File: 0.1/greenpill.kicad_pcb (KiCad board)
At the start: 4 copper layers, 20 x 55.1 mm, 31 parts, among them J1 Conn_01x20_Male, J2 Conn_01x20_Male, J3 Conn_01x04_Male, J5 USB_C_Receptacle_USB2.0, SW1 SW_Push, SW2 SW_Push, U1 ATSAMD51G18A-M, U2 MIC5504-3.3YM5, U3 S25FL064, Y1 Crystal_GND23

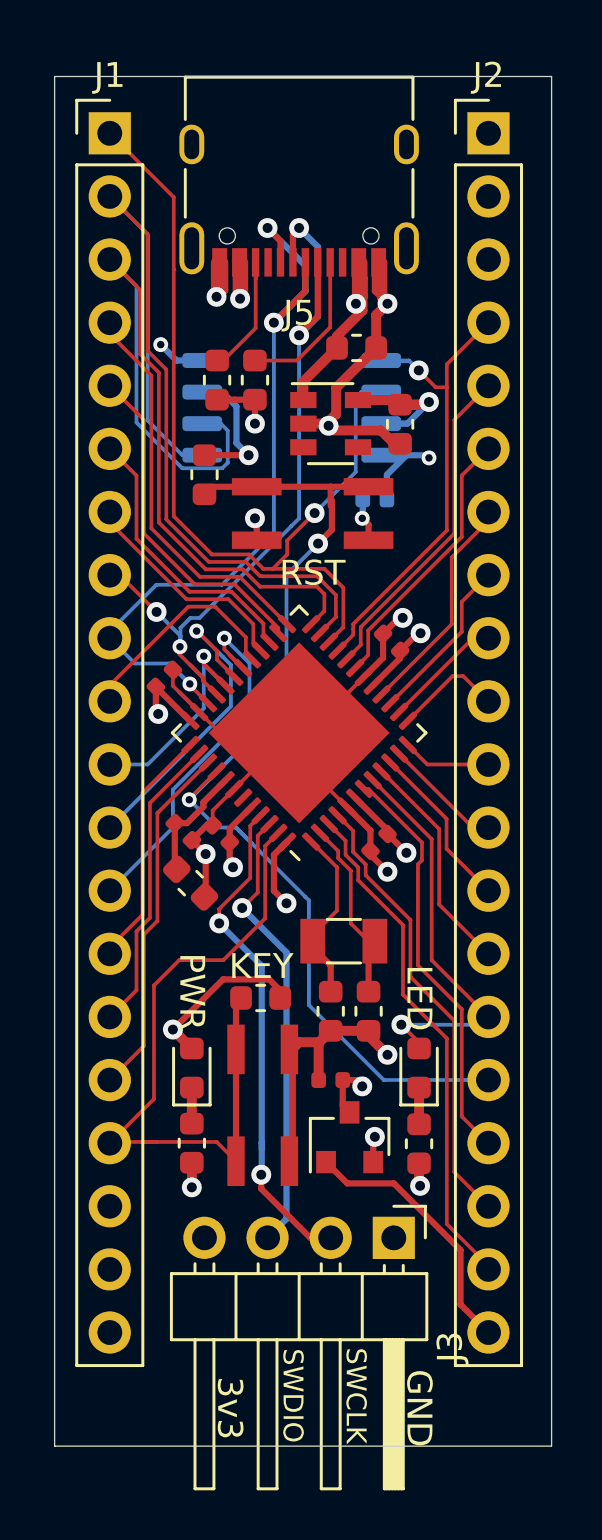
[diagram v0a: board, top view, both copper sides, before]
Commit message: Trimmed board, added pinout silkscreen
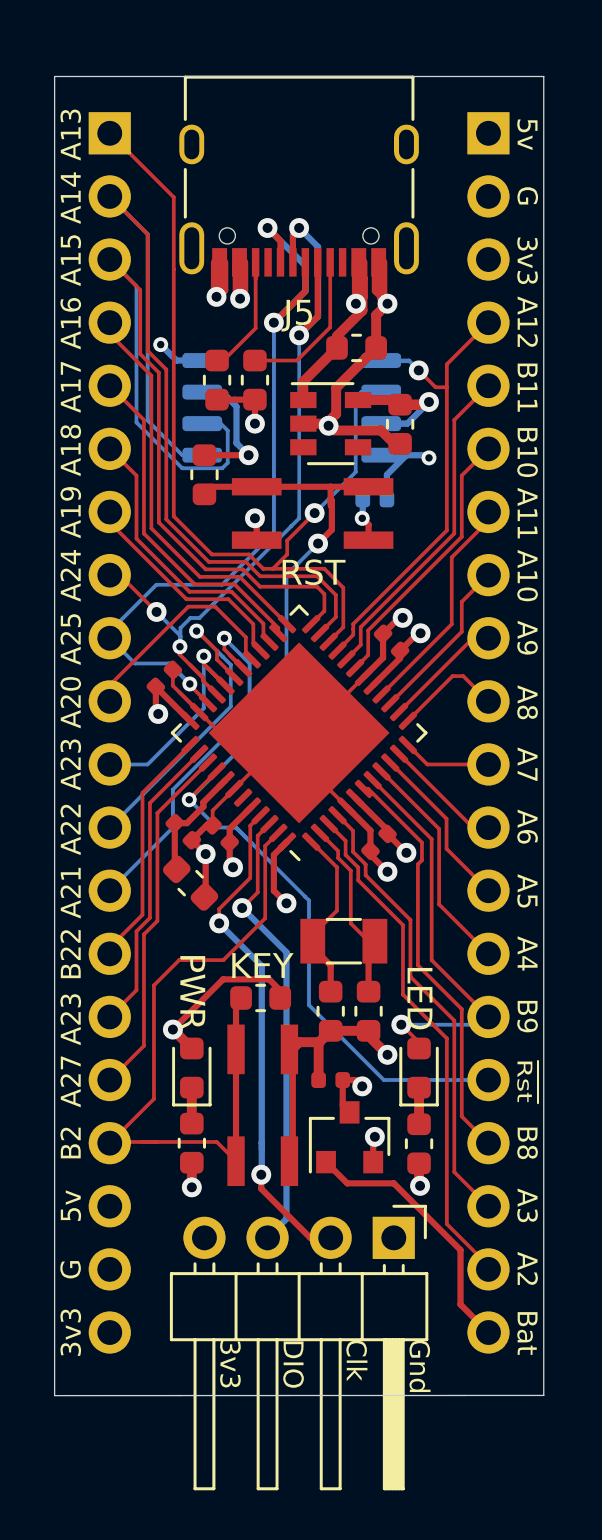
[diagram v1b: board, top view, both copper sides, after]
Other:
- board size 20 x 55.1 mm -> 19.7 x 53.1 mm
- board text added: "5v"
- board text added: "A10"
- board text added: "A11"
- board text added: "A12"
- board text added: "A13"
- board text added: "A14"
- board text added: "A15"
- board text added: "A16"
- board text added: "A17"
- board text added: "A18"
- board text added: "A19"
- board text added: "A2"
- board text added: "A20"
- board text added: "A21"
- board text added: "A22"
- board text added: "A23"
- board text added: "A24"
- board text added: "A25"
- board text added: "A27"
- board text added: "A3"
- board text added: "A4"
- board text added: "A5"
- board text added: "A6"
- board text added: "A7"
- board text added: "A8"
- board text added: "A9"
- board text added: "B10"
- board text added: "B11"
- board text added: "B2"
- board text added: "B22"
- board text added: "B8"
- board text added: "B9"
- board text added: "Bat"
- board text added: "Clk"
- board text added: "DIO"
- board text added: "G"
- board text added: "Gnd"
- board text added: "Rst"
- board text removed: "GND"
- board text removed: "SWCLK"
- board text removed: "SWDIO"

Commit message: PINOUT CHANGE, rerouted and updated silk.s
Swapped left pins 13 and 16 (formerly A21 & A27 respectively) so PWM output on A21 can be used for Textier LED4:G. A27 now on pin L13 is used for key matrix scanning and so doesn't require PWM
Rerouted only affected traces
Swapped silkscreen labels
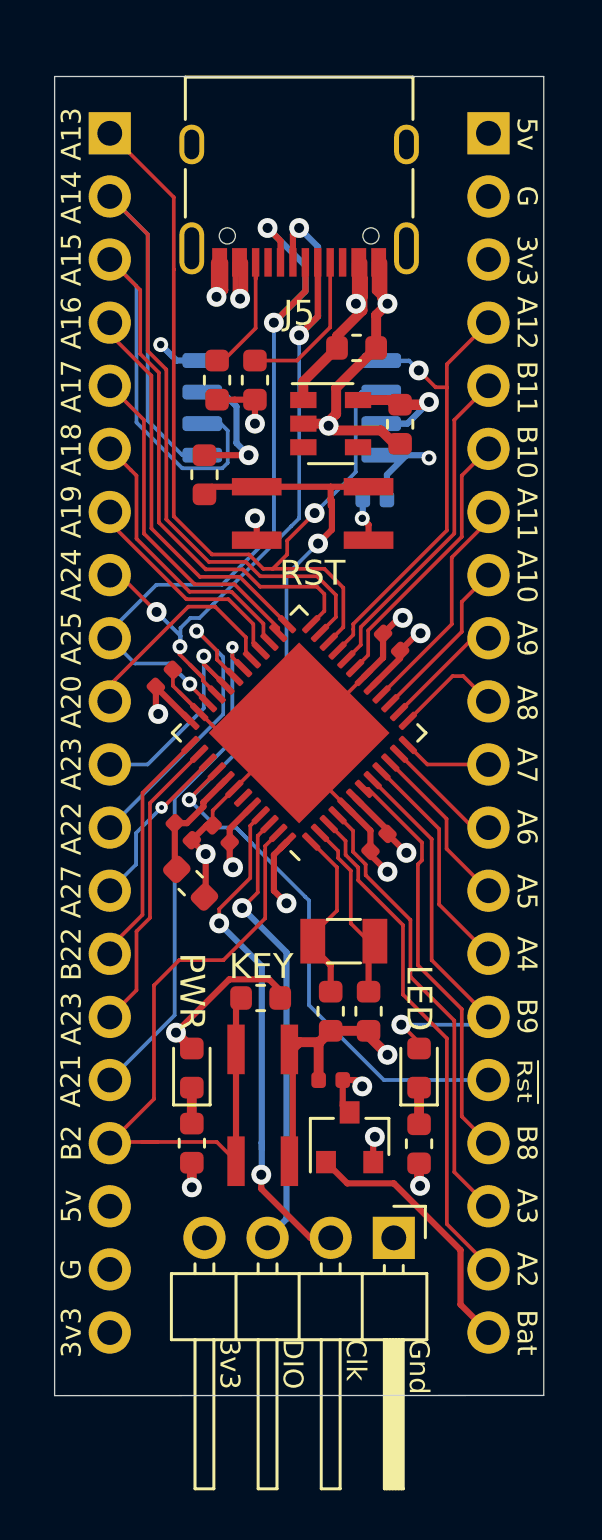
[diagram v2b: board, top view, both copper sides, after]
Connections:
- J1 pad 13: /pa21 -> /pa27
- J1 pad 16: /pa27 -> /pa21
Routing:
- net /pa27: track 14.4 -> 6.89 mm, vias 0 -> 1
- net /pa21: track 15.2 -> 20.5 mm
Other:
- net class Default: clearance 0.15 -> 0.09; trace_width 0.25 -> 0.09; via_dia 0.8 -> 0.5; via_drill 0.4 -> 0.2
- rule trace_clearance: 0.15 -> 0.09
- rule trace_min: 0.127 -> 0.09
- rule via_min_drill: 0.3 -> 0.2
- rule via_min_size: 0.4 -> 0.45

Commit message: a bit of tweaking
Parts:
- C7, C8: value 1u -> 10u
- moved R2 7.70 mm to (140.0, 83.0)
- moved U2 4.89 mm to (132.7, 83.4), turned to 270 degrees
- moved R1 4.71 mm to (138.4, 83.0)
- moved C8 3.92 mm to (136.1, 84.4), turned to 0 degrees
- moved C7 1.97 mm to (136.1, 82.2)
- moved SW1 1.46 mm to (136.4, 88.0)
- moved R5 0.23 mm to (132.0, 87.7), turned to 90 degrees
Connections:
- R6 pad 2: /pb02 -> /pa02
- SW2 pad 1: /pb02 -> /pa02
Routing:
- net /pa02: track 20.6 -> 42.1 mm, vias 0 -> 1
- net /cc2: track 5.16 -> 15.2 mm
- net /pb02: track 29.3 -> 26.3 mm
- net /pa12: track 20.0 -> 21.8 mm, vias 1 -> 0
- net +3V3: track 123.4 -> 125.2 mm, vias 9 -> 10
- net /pa25: track 33.0 -> 31.5 mm
- net /pa13: track 36.3 -> 37.7 mm
- net /pa24: track 32.3 -> 31.1 mm
- net /cc1: track 5.94 -> 5.06 mm
- net /pa15: track 34.6 -> 34.0 mm
- net +5V: track 66.4 -> 67.0 mm, vias 2 -> 3
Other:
- board text added: "1"
- board text added: "10"
- board text added: "11"
- board text added: "12"
- board text added: "13"
- board text added: "14"
- board text added: "15"
- board text added: "16"
- board text added: "17"
- board text added: "18"
- board text added: "19"
- board text added: "2"
- board text added: "20"
- board text added: "21"
- board text added: "22"
- board text added: "23"
- board text added: "24"
- board text added: "25"
- board text added: "26"
- board text added: "27"
- board text added: "28"
- board text added: "29"
- board text added: "3"
- board text added: "30"
- board text added: "31"
- board text added: "32"
- board text added: "4"
- board text added: "5"
- board text added: "6"
- board text added: "7"
- board text added: "8"
- board text added: "9"

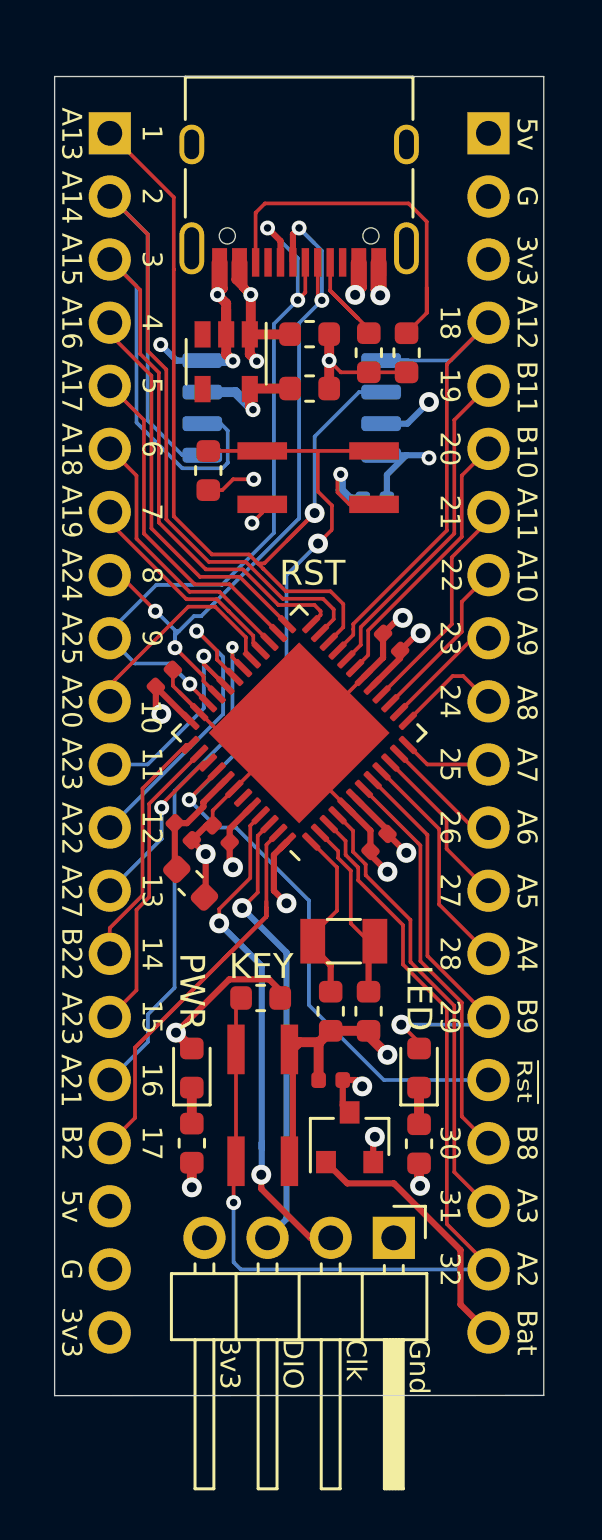
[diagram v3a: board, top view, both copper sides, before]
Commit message: Switched to QFN-64 package, reassigned pins. Trimmed Edge.Cuts
Still TODO:
 - Redo silkscreen
 - Move passives near MCU to optimal position (1v2 caps especially)
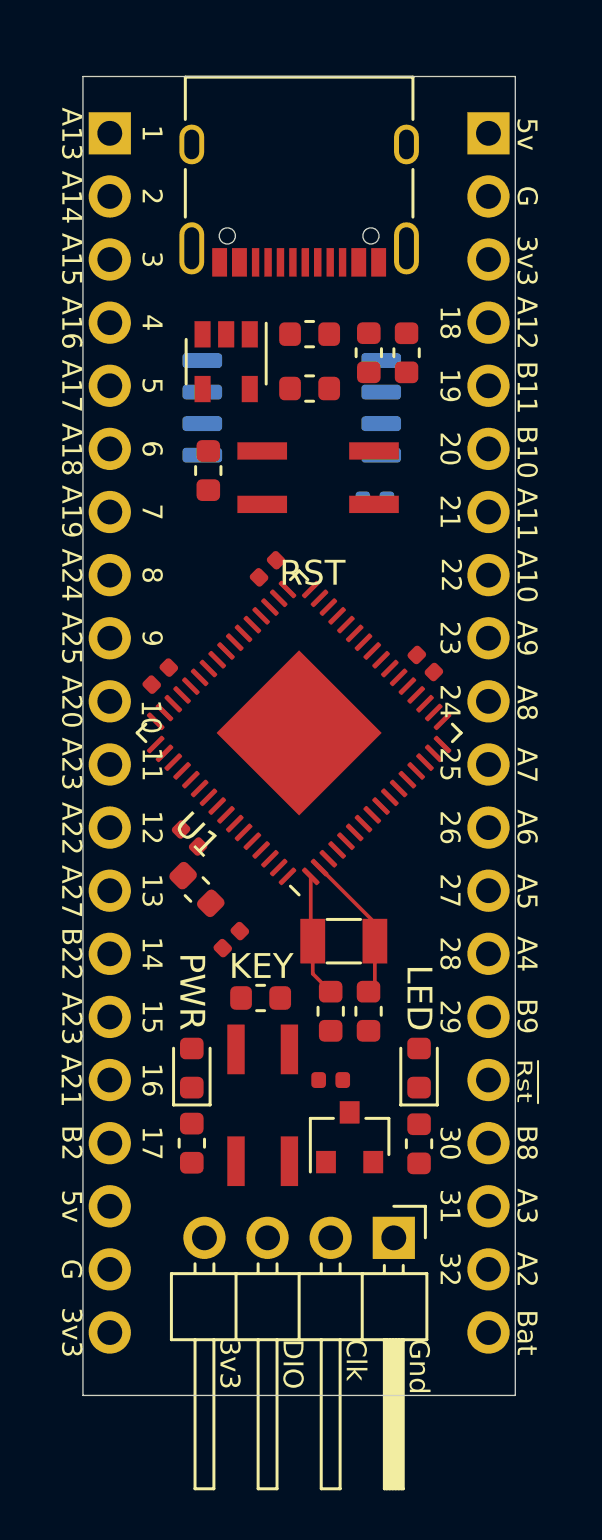
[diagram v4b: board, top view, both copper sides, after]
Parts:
- U1: value ATSAMD51G18A-M -> ATSAMD51J18A-M; footprint Package_DFN_QFN:QFN-48-1EP_7x7mm_P0.5mm_EP5.15x5.15mm -> Package_DFN_QFN:QFN-64-1EP_9x9mm_P0.5mm_EP4.7x4.7mm
- moved C4 11.1 mm to (130.0, 96.0), turned to 45 degrees
- moved C1 6.06 mm to (134.4, 91.7)
- moved C2 4.27 mm to (132.9, 106.6), turned to 225 degrees
- moved C6 1.60 mm to (140.7, 95.5)
- moved C5 0.36 mm to (131.5, 104.6)
- moved C3 0.36 mm to (131.2, 102.5)
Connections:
- D2 pad 2: /pb09 -> /pb04
- J1 pad 1: /pa13 -> /pa16
- J1 pad 10: /pa20 -> /pa22
- J1 pad 11: /pa23 -> /pb22
- J1 pad 12: /pa22 -> /pb23
- J1 pad 14: /pb22 -> /pb31
- J1 pad 15: /pb23 -> /pb00
- J1 pad 16: /pa21 -> /pb01
- J1 pad 2: /pa14 -> /pa17
- J1 pad 3: /pa15 -> /pa18
- J1 pad 4: /pa16 -> /pa19
- J1 pad 5: /pa17 -> /pb16
- J1 pad 6: /pa18 -> /pb17
- J1 pad 7: /pa19 -> /pa20
- J2 pad 15: /pb09 -> /pa02
- J2 pad 17: /pb08 -> /pb30
- J2 pad 19: /pa02 -> /pb04
- J2 pad 4: /pa12 -> /pb13
- J2 pad 5: /pb11 -> /pb12
- J2 pad 6: /pb10 -> /pb11
- J2 pad 7: /pa11 -> /pb10
- U1 pad 10: /pa05 -> /pb07
- U1 pad 11: /pa06 -> /pb08
- U1 pad 12: /pa07 -> /pb09
- U1 pad 13: /pa08 -> /pa04
- U1 pad 14: /pa09 -> /pa05
- U1 pad 15: /pa10 -> /pa06
- U1 pad 16: /pa11 -> /pa07
- U1 pad 17: +3V3 -> /pa08
- U1 pad 18: GND -> /pa09
- U1 pad 19: /pb10 -> /pa10
- U1 pad 20: /pb11 -> /pa11
- U1 pad 21: /pa12 -> +3V3
- U1 pad 22: /pa13 -> GND
- U1 pad 23: /pa14 -> /pb10
- U1 pad 24: /pa15 -> /pb11
- U1 pad 25: /pa16 -> /pb12
- U1 pad 26: /pa17 -> /pb13
- U1 pad 27: /pa18 -> /pb14
- U1 pad 28: /pa19 -> /pb15
- U1 pad 29: /pa20 -> /pa12
- U1 pad 30: /pa21 -> /pa13
- U1 pad 31: /pa22 -> /pa14
- U1 pad 32: /pa23 -> /pa15
- U1 pad 33: /pa24 -> GND
- U1 pad 34: /pa25 -> +3V3
- U1 pad 35: GND -> /pa16
- U1 pad 36: +3V3 -> /pa17
- U1 pad 37: /pb22 -> /pa18
- U1 pad 38: /pb23 -> /pa19
- U1 pad 39: /pa27 -> /pb16
- U1 pad 40: /!reset -> /pb17
- U1 pad 41: +1V2 -> /pa20
- U1 pad 42: GND -> /pa21
- U1 pad 43: /vsw -> /pa22
- U1 pad 44: +3V3 -> /pa23
- U1 pad 45: /pa30 -> /pa24
- U1 pad 46: /pa31 -> /pa25
- U1 pad 47: /pb02 -> GND
- U1 pad 48: /pb03 -> +3V3
- U1 pad 49: GND -> /pb22
- U1 pad 5: GND -> /pb04
- U1 pad 6: +3V3 -> /pb05
- U1 pad 7: /pb08 -> GND
- U1 pad 8: /pb09 -> Net-(U1-Pad8)
- U1 pad 9: /pa04 -> /pb06
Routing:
- net +3V3: track 125.2 -> 0.00 mm, vias 10 -> 0
- net GND: track 67.6 -> 0.00 mm, vias 13 -> 0
- net +5V: track 67.0 -> 0.00 mm, vias 3 -> 0
- net /!reset: track 44.1 -> 0.00 mm, vias 2 -> 0
- net /pa02: track 42.1 -> 0.00 mm, vias 1 -> 0
- net /pa13: track 37.7 -> 0.00 mm, vias 1 -> 0
- net /pa14: track 35.8 -> 0.00 mm
- net /pa15: track 34.0 -> 0.00 mm
- net /pa25: track 31.5 -> 0.00 mm, vias 3 -> 0
- net /pa24: track 31.1 -> 0.00 mm, vias 4 -> 0
- net /pb02: track 26.3 -> 0.00 mm
- net /pa12: track 21.8 -> 0.00 mm
- net /pa30: track 21.2 -> 0.00 mm, vias 2 -> 0
- net /pa21: track 20.7 -> 0.00 mm, vias 1 -> 0
- net /pa03: track 18.3 -> 0.00 mm
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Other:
- board size 19.7 x 53.1 mm -> 17.4 x 53.1 mm

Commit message: Routed trivial IOs
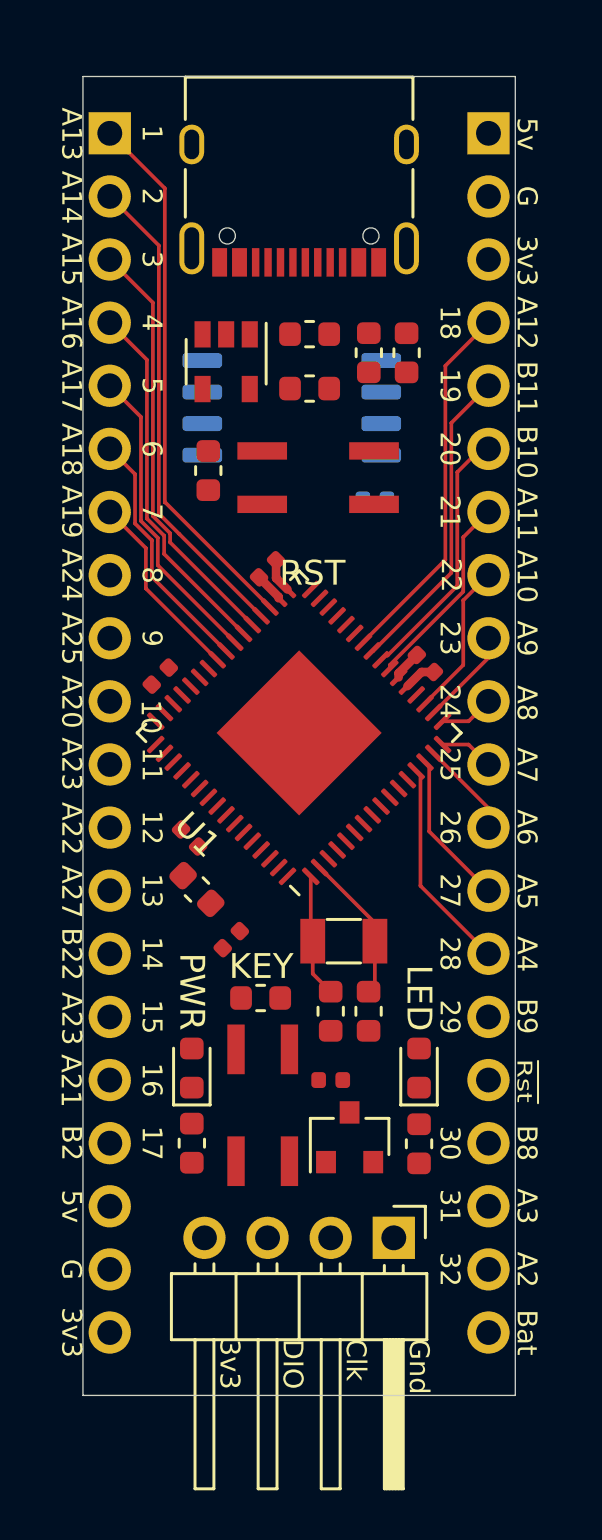
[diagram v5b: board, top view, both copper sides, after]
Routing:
- net /pa16: track 0.00 -> 21.8 mm
- net /pa17: track 0.00 -> 19.4 mm
- net /pa18: track 0.00 -> 17.1 mm
- net /pb13: track 0.00 -> 14.9 mm
- net /pa19: track 0.00 -> 14.7 mm
- net /pb12: track 0.00 -> 12.6 mm
- net /pb16: track 0.00 -> 12.4 mm
- net /pb11: track 0.00 -> 10.5 mm
- net /pb17: track 0.00 -> 10.1 mm
- net /pa04: track 0.00 -> 8.57 mm
- net /pb10: track 0.00 -> 7.94 mm
- net /pa20: track 0.00 -> 7.74 mm
- net /pa05: track 0.00 -> 6.23 mm
- net /pa10: track 0.00 -> 6.23 mm
- net /pa06: track 0.00 -> 3.90 mm
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
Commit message: yeet
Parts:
- moved C2 3.82 mm to (131.8, 102.9), turned to 315 degrees
- moved R6 1.98 mm to (132.1, 109.1), turned to 0 degrees
- moved C5 1.62 mm to (130.5, 103.3)
- moved C3 1.14 mm to (130.5, 101.7)
- moved C9 0.27 mm to (137.2, 112.2)
- moved Y1 0.19 mm to (137.2, 106.7)
- moved C6 0.06 mm to (140.8, 95.5)
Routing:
- net +3V3: track 2.47 -> 100.8 mm, vias 0 -> 12
- net +5V: track 0.00 -> 76.8 mm, vias 0 -> 2
- net GND: track 2.57 -> 75.2 mm, vias 0 -> 13
- net /!reset: track 0.00 -> 43.6 mm, vias 0 -> 4
- net /pa25: track 0.00 -> 30.3 mm, vias 0 -> 2
- net /pa24: track 0.00 -> 28.3 mm, vias 0 -> 3
- net /pa30: track 0.00 -> 25.7 mm, vias 0 -> 1
- net /pa02: track 0.00 -> 23.1 mm, vias 0 -> 2
- net /pb04: track 0.00 -> 22.1 mm, vias 0 -> 2
- net /pa31: track 0.00 -> 21.9 mm, vias 0 -> 1
- net /pb30: track 0.00 -> 19.9 mm, vias 0 -> 1
- net /pa03: track 0.00 -> 17.0 mm, vias 0 -> 1
- net /pb03: track 0.00 -> 13.9 mm, vias 0 -> 2
- net /pb02: track 0.00 -> 13.9 mm
- net /pa12: track 0.00 -> 13.5 mm, vias 0 -> 1
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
